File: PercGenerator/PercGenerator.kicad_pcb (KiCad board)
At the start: 2 copper layers, 94 x 25.4 mm, 17 parts, among them J1 Conn_01x09_Male, J2 Conn_01x02_Male, Q1 2N3904, U1 LM741

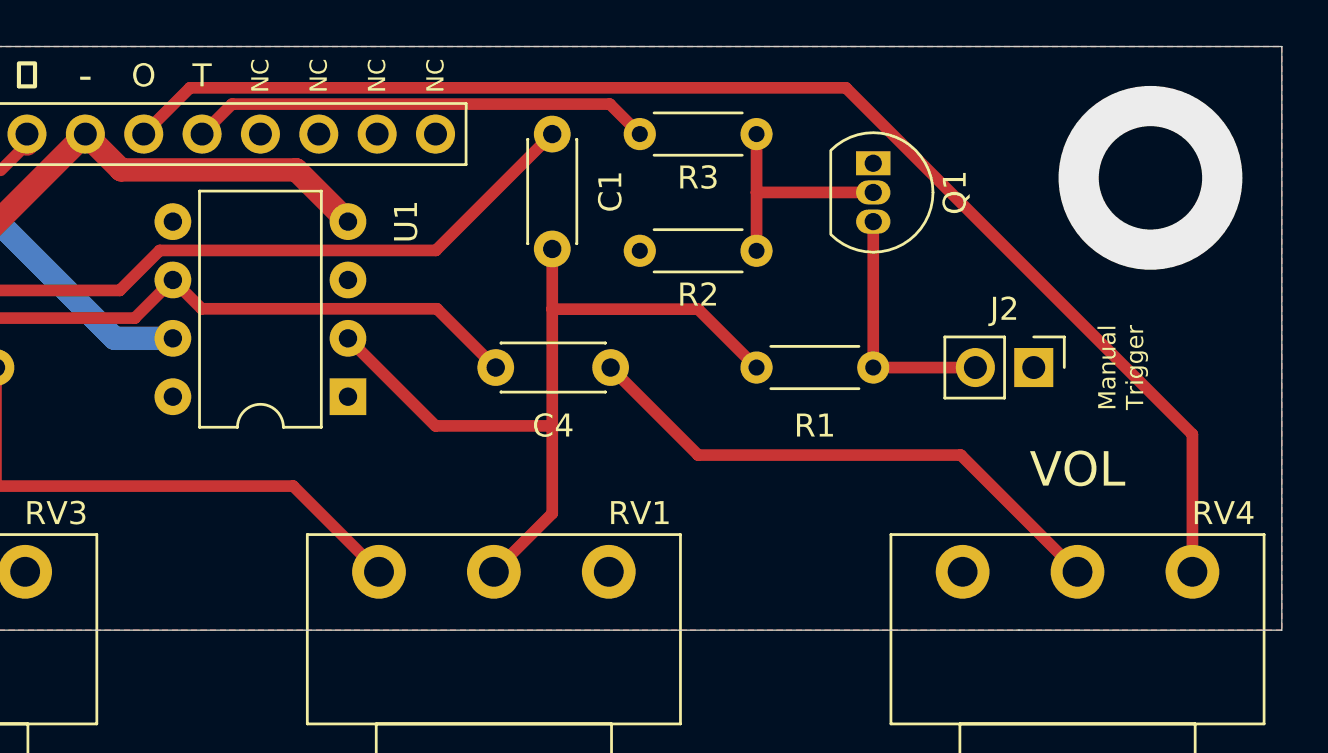
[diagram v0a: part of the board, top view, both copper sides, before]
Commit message: Added panel dimensions, changed Perc Volume pot
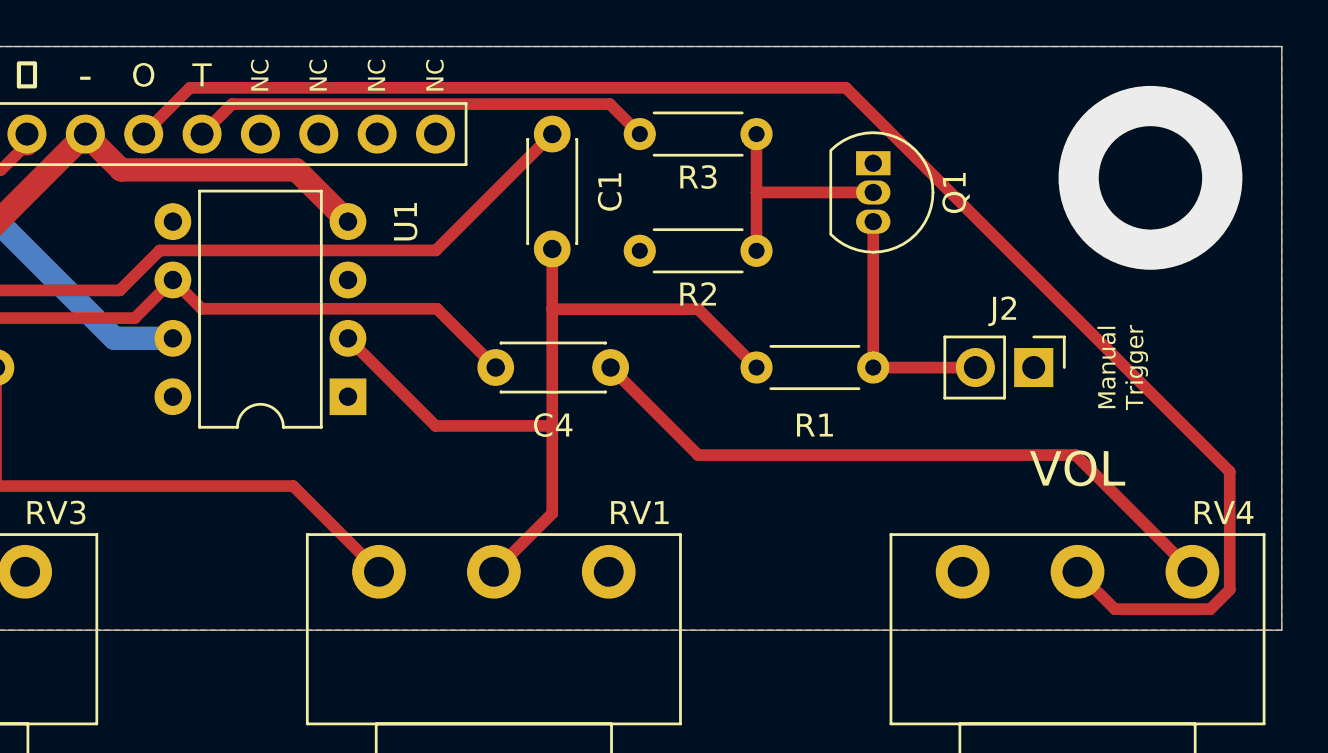
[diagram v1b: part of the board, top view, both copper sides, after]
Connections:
- RV4 pad 2: Net-(C4-Pad1) -> /OUT
- RV4 pad 3: /OUT -> Net-(C4-Pad1)
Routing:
- net /OUT: track 58.7 -> 67.8 mm
- net Net-(C4-Pad1): track 24.0 -> 29.0 mm

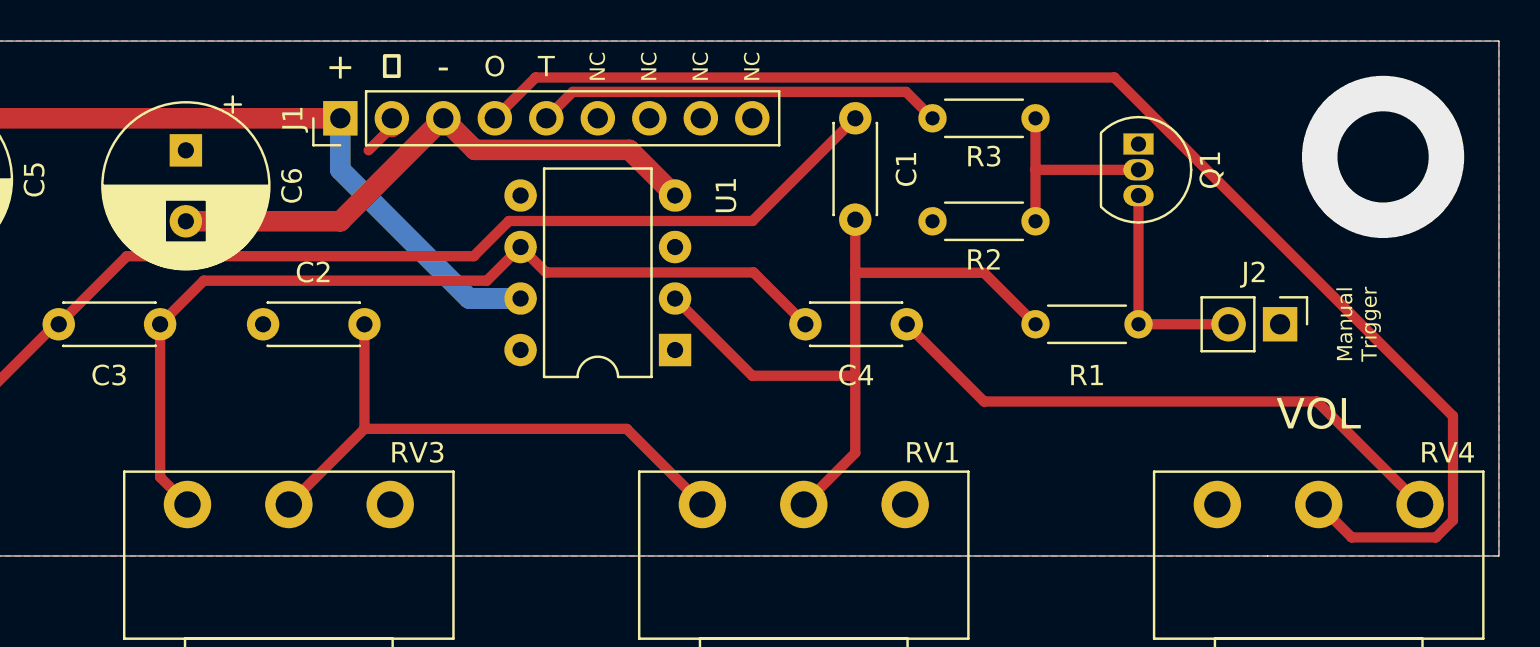
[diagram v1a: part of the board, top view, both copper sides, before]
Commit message: Resolved Issue #3 Also: * Added output cap to 555 modules * EnvelopeFilter now has an output cap
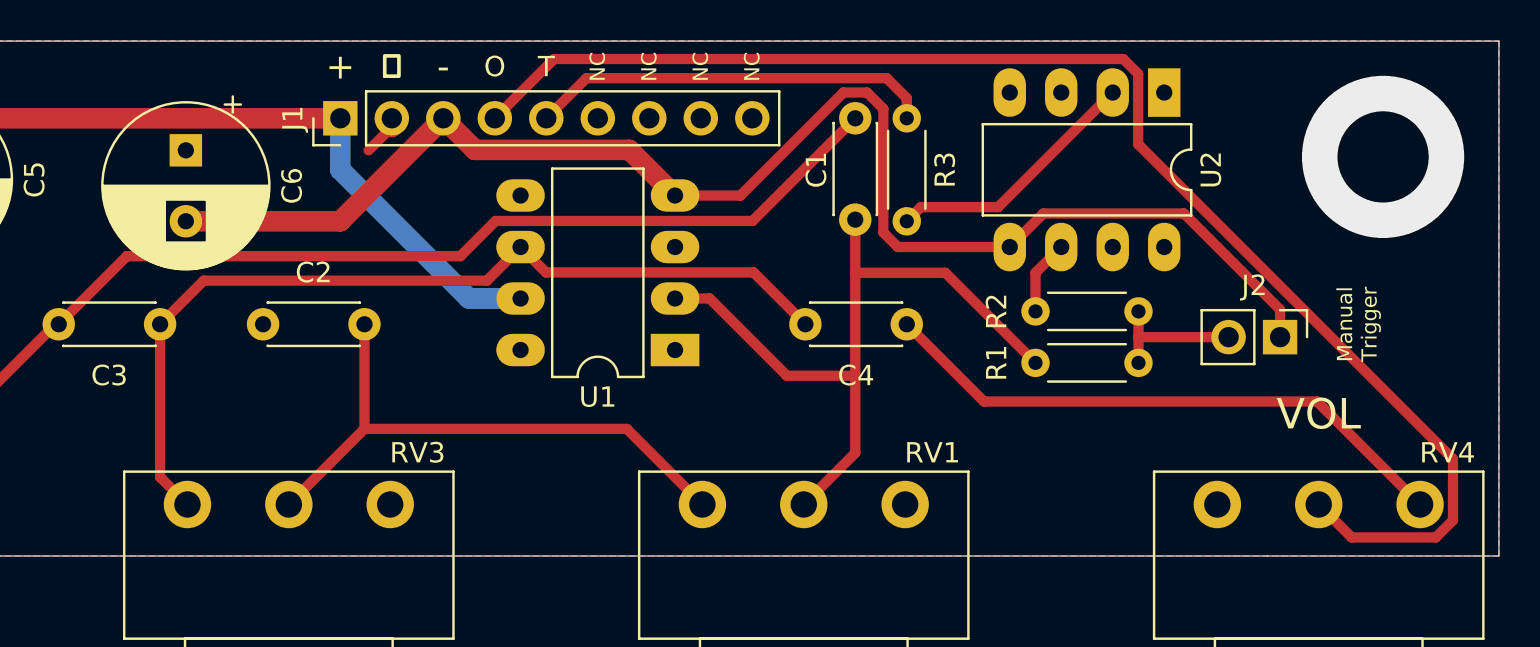
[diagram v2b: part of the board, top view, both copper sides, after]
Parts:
- removed Q1: 2N3904, Package_TO_SOT_THT:TO-92_Inline
- added U2: 6N139, Package_DIP:DIP-8_W7.62mm_LongPads, F.Cu at (213.4, 121.9)
- C2: value 0.001uF -> 0.01uF
- R2: value 10k -> 1k
- R3: value 10k -> 270
- RV1, RV3: value 1M -> 100k
- U1: footprint Package_DIP:DIP-8_W7.62mm -> Package_DIP:DIP-8_W7.62mm_LongPads
- moved R2 6.75 mm to (212.1, 132.7)
- moved R1 1.91 mm to (207.0, 135.3)
- moved R3 1.27 mm to (200.7, 123.2), turned to 270 degrees
- moved J2 0.64 mm to (219.1, 134.0)
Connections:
- J2 pad 1: GND -> -15V
- R2 pad 1: Net-(Q1-Pad2) -> Net-(J2-Pad2)
- R2 pad 2: GND -> Net-(R2-Pad2)
- R3 pad 2: Net-(Q1-Pad2) -> Net-(R3-Pad2)
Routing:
- net -15V: track 27.8 -> 70.5 mm
- net Net-(R3-Pad2): track 0.00 -> 12.8 mm
- net Net-(Q1-Pad2): track 10.2 -> 0.00 mm
- net Net-(J2-Pad2): track 10.8 -> 6.98 mm
- net Net-(R2-Pad2): track 0.00 -> 3.70 mm
- net /OUT: track 67.8 -> 69.3 mm
- net Net-(C1-Pad2): track 35.5 -> 36.3 mm
